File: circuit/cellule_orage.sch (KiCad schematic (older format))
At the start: 62 parts, among them Q1 BSS138, Q2 BSS138, Q3 BSS138, SW1 OFF/ON, U2 TLC274, U4 LM555N, U5 TLP291

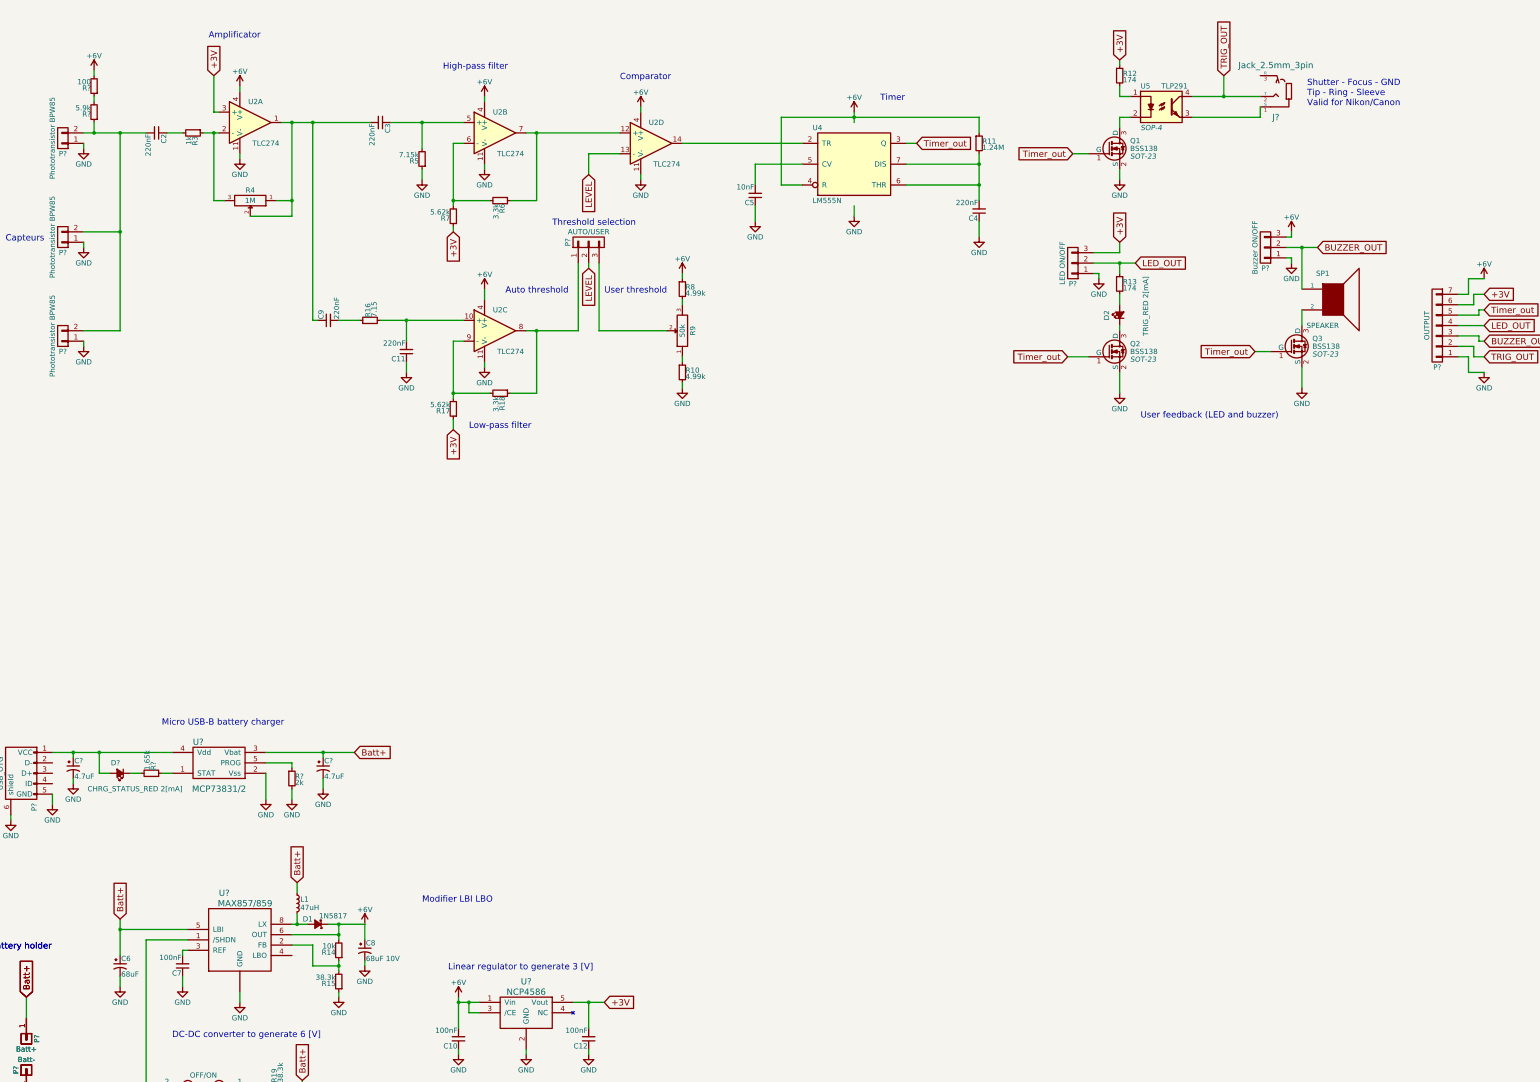
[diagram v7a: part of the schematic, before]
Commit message: Added LBI infos
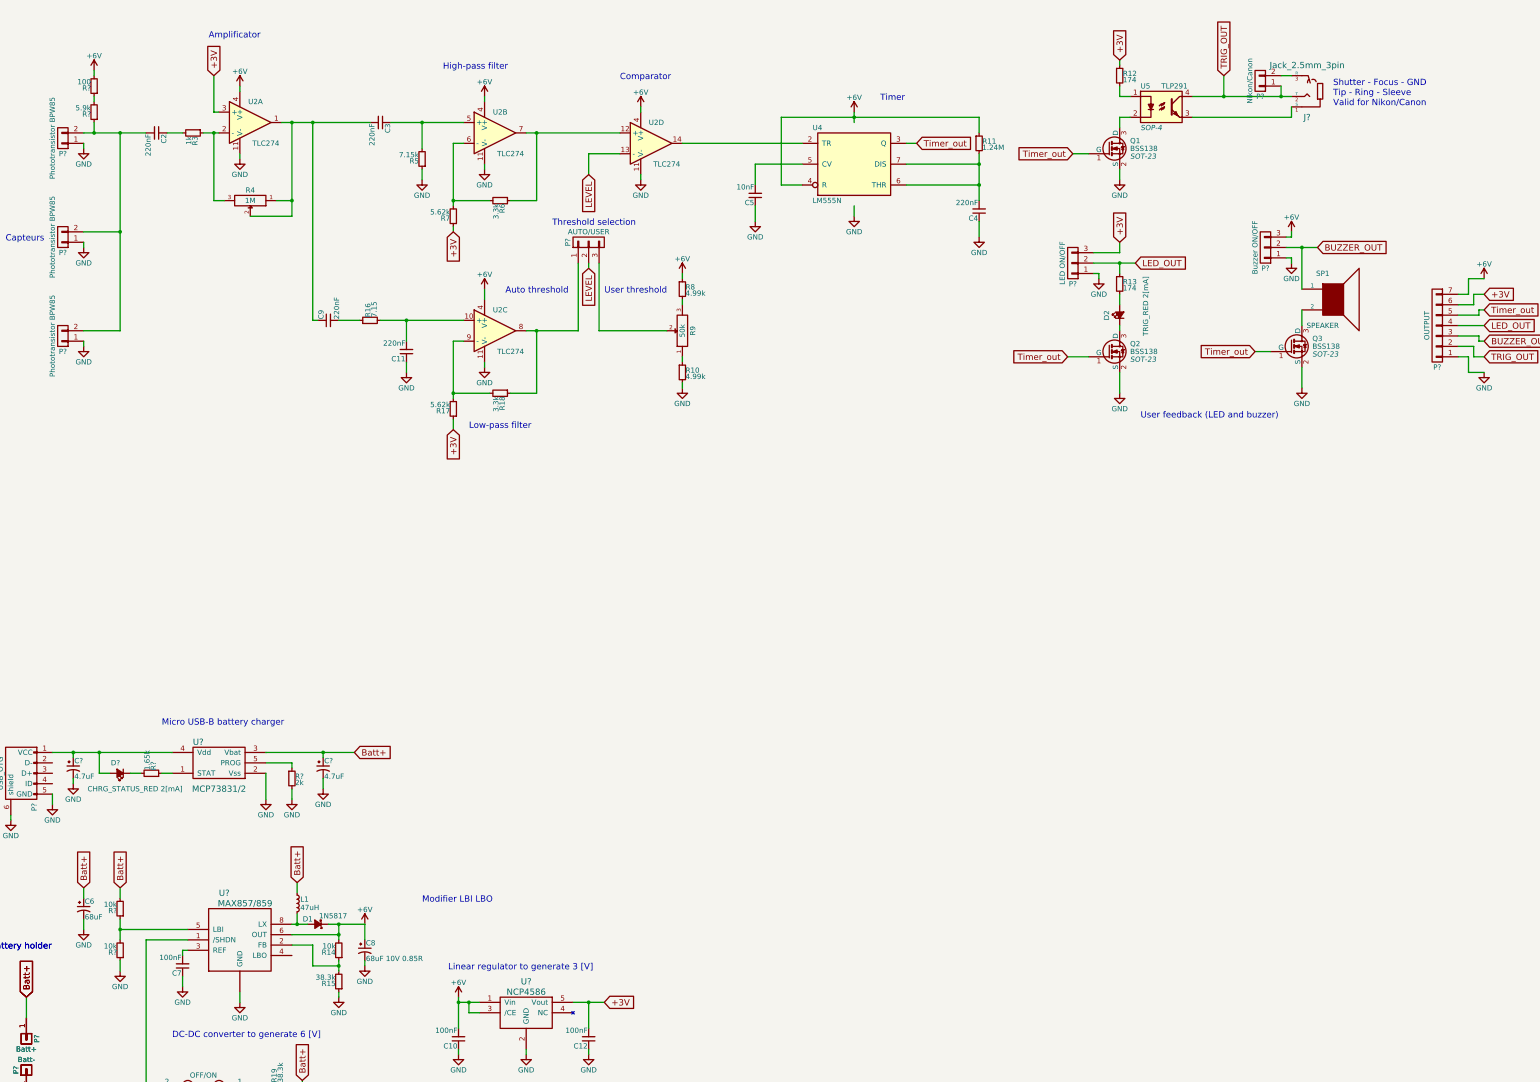
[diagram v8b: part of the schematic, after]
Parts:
- added P?: Nikon/Canon, symbol CONN_01X02
- added R? (x2): 10k, symbol R_Small
- C8: value 68uF 10V -> 68uF 10V 0.85R
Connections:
- net Batt+: now also R?.2; no longer U?.5 (LBI)
- net GND: now also R?.1
- net TRIG_OUT: now also P?.1 (P1)
- net at J?.3 (R): now also P?.2 (P2)
- new net: R?.1, R?.2, U?.5 (LBI)
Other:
- moved on the sheet: C6, J?
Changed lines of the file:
@@
 Wire Wire Line
 	10900 1800 11050 1800
-Text Notes 13150 1350 0    60   ~ 0
+Text Notes 13400 1350 0    60   ~ 0
 Shutter - Focus - GND\nTip - Ring - Sleeve\nValid for Nikon/Canon
-Wire Wire Line
-	12050 1250 12700 1250
-Wire Wire Line
-	12050 1450 12700 1450
 Text GLabel 10850 3750 0    60   Input ~ 0
 Timer_out
@@
 L CP1_Small C6
 U 1 1 57875685
-P 1750 9600
-F 0 "C6" H 1760 9670 50  0000 L CNN
-F 1 "68uF" H 1760 9520 50  0000 L CNN
-F 2 "" H 1750 9600 50  0000 C CNN
-F 3 "" H 1750 9600 50  0000 C CNN
-	1    1750 9600
+P 1400 9050
+F 0 "C6" H 1410 9120 50  0000 L CNN
+F 1 "68uF" H 1410 8970 50  0000 L CNN
+F 2 "" H 1400 9050 50  0000 C CNN
+F 3 "" H 1400 9050 50  0000 C CNN
+	1    1400 9050
 	1    0    0    -1
 $EndComp
@@
 P 4100 9450
 F 0 "C8" H 4110 9520 50  0000 L CNN
-F 1 "68uF 10V" H 4110 9370 50  0000 L CNN
+F 1 "68uF 10V 0.85R" H 4110 9370 50  0000 L CNN
 F 2 "" H 4100 9450 50  0000 C CNN
 F 3 "" H 4100 9450 50  0000 C CNN
@@
 Wire Wire Line
 	13100 3300 13100 3450
-Text GLabel 1750 9150 1    60   Input ~ 0
+Text GLabel 1750 8850 1    60   Input ~ 0
 Batt+
 Text GLabel 6400 9950 2    60   Input ~ 0
@@
 Wire Wire Line
 	2350 9800 2350 9700
-Wire Wire Line
-	1750 9150 1750 9500
-Wire Wire Line
-	2400 9250 1750 9250
-Connection ~ 1750 9250
 $Comp
 L GND #PWR1
 U 1 1 57881958
-P 1750 9800
-F 0 "#PWR1" H 1750 9550 50  0001 C CNN
-F 1 "GND" H 1750 9650 50  0000 C CNN
-F 2 "" H 1750 9800 50  0000 C CNN
-F 3 "" H 1750 9800 50  0000 C CNN
-	1    1750 9800
-	1    0    0    -1
-$EndComp
-Wire Wire Line
-	1750 9700 1750 9800
+P 1750 9650
+F 0 "#PWR1" H 1750 9400 50  0001 C CNN
+F 1 "GND" H 1750 9500 50  0000 C CNN
+F 2 "" H 1750 9650 50  0000 C CNN
+F 3 "" H 1750 9650 50  0000 C CNN
+	1    1750 9650
+	1    0    0    -1
+$EndComp
 Wire Wire Line
 	2350 9500 2350 9450
@@
 L Jack_3.5mm_3pin J?
 U 1 1 57F68248
-P 12850 1200
-F 0 "J?" H 12850 1450 60  0000 C CNN
-F 1 "Jack_2.5mm_3pin" H 12850 950 60  0000 C CNN
-F 2 "" H 12850 1200 60  0000 C CNN
-F 3 "" H 12850 1200 60  0000 C CNN
-	1    12850 1200
+P 13150 1200
+F 0 "J?" H 13150 1450 60  0000 C CNN
+F 1 "Jack_2.5mm_3pin" H 13150 950 60  0000 C CNN
+F 2 "" H 13150 1200 60  0000 C CNN
+F 3 "" H 13150 1200 60  0000 C CNN
+	1    13150 1200
 	1    0    0    1
 $EndComp
@@
 Modifier LBI LBO
 Wire Wire Line
-	12700 1450 12700 1350
-Wire Wire Line
 	12350 1050 12350 1250
 Connection ~ 12350 1250
+$Comp
+L CONN_01X02 P?
+U 1 1 57FD01E4
+P 12700 1100
+F 0 "P?" H 12700 1250 50  0000 C CNN
+F 1 "Nikon/Canon" V 12800 1100 50  0000 C CNN
+F 2 "" H 12700 1100 50  0000 C CNN
+F 3 "" H 12700 1100 50  0000 C CNN
+	1    12700 1100
+	-1   0    0    1
+$EndComp
+Wire Wire Line
+	12900 1050 13000 1050
+Wire Wire Line
+	12900 1150 12900 1250
+Connection ~ 12900 1250
+Wire Wire Line
+	12050 1250 13000 1250
+Wire Wire Line
+	12050 1450 13000 1450
+Wire Wire Line
+	13000 1450 13000 1350
+$Comp
+L GND #PWR?
+U 1 1 57FD5DF3
+P 1400 9250
+F 0 "#PWR?" H 1400 9000 50  0001 C CNN
+F 1 "GND" H 1400 9100 50  0000 C CNN
+F 2 "" H 1400 9250 50  0000 C CNN
+F 3 "" H 1400 9250 50  0000 C CNN
+	1    1400 9250
+	1    0    0    -1
+$EndComp
+$Comp
+L R_Small R?
+U 1 1 57FD5F06
+P 1750 9050
+F 0 "R?" H 1780 9070 50  0000 L CNN
+F 1 "10k" H 1780 9010 50  0000 L CNN
+F 2 "" H 1750 9050 50  0000 C CNN
+F 3 "" H 1750 9050 50  0000 C CNN
+	1    1750 9050
+	-1   0    0    1
+$EndComp
+$Comp
+L R_Small R?
+U 1 1 57FD603B
+P 1750 9450
+F 0 "R?" H 1780 9470 50  0000 L CNN
+F 1 "10k" H 1780 9410 50  0000 L CNN
+F 2 "" H 1750 9450 50  0000 C CNN
+F 3 "" H 1750 9450 50  0000 C CNN
+	1    1750 9450
+	-1   0    0    1
+$EndComp
+Text GLabel 1400 8850 1    60   Input ~ 0
+Batt+
+Wire Wire Line
+	1400 8850 1400 8950
+Wire Wire Line
+	1400 9150 1400 9250
+Wire Wire Line
+	1750 8850 1750 8950
+Wire Wire Line
+	1750 9150 1750 9350
+Wire Wire Line
+	1750 9550 1750 9650
+Wire Wire Line
+	2400 9250 1750 9250
+Connection ~ 1750 9250
 $EndSCHEMATC
